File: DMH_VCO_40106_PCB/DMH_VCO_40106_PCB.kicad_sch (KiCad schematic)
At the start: 0 parts

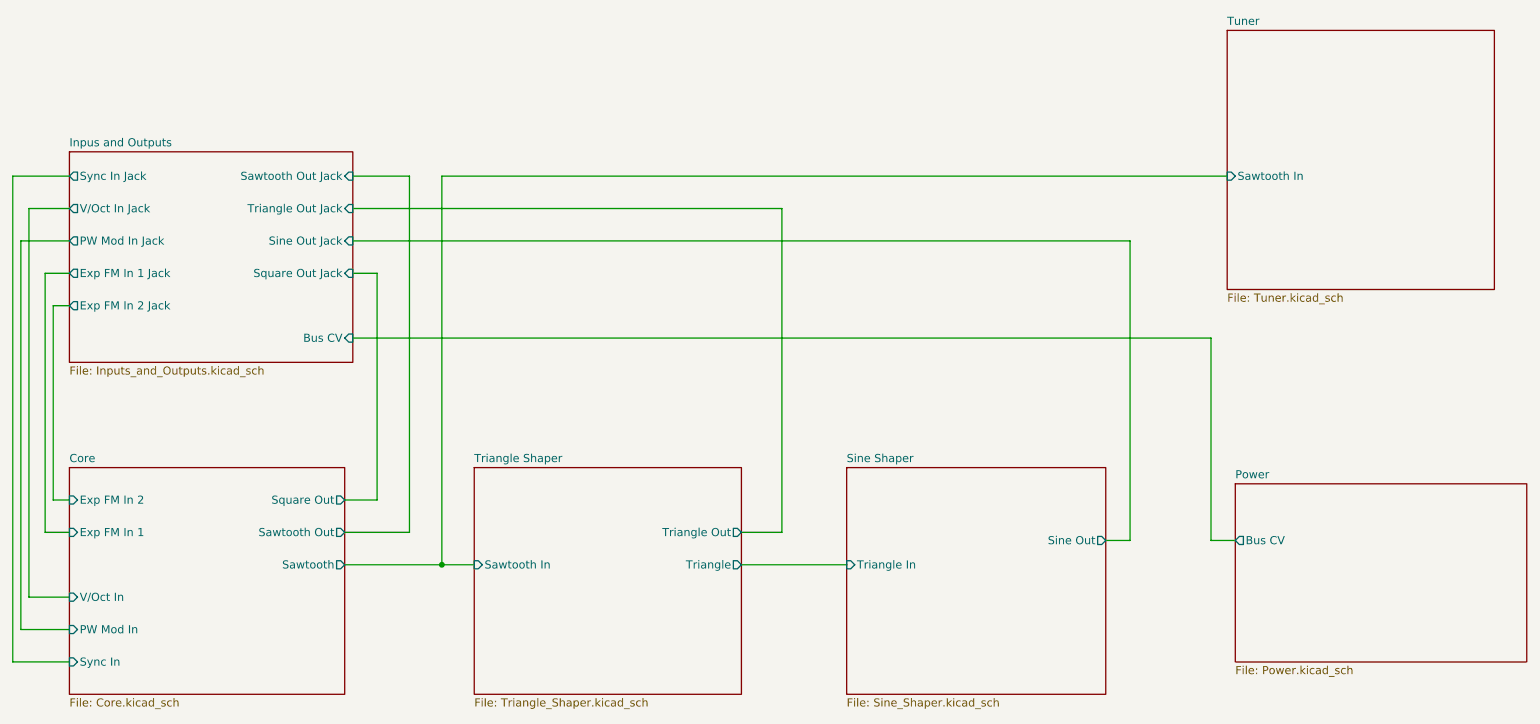
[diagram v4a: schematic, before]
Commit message: FW work in progress
Code left in state where fixed frequency point (e.g. 300Hz) is recognized, and the tuner swings from TOO LOW to TOO HIGH depending if below or above this frequency. I see a ~+10Hz offset though if checking the frequency in ableton. Also had to connect uc to square wave. Saw wave is too unstable without hysteresis.
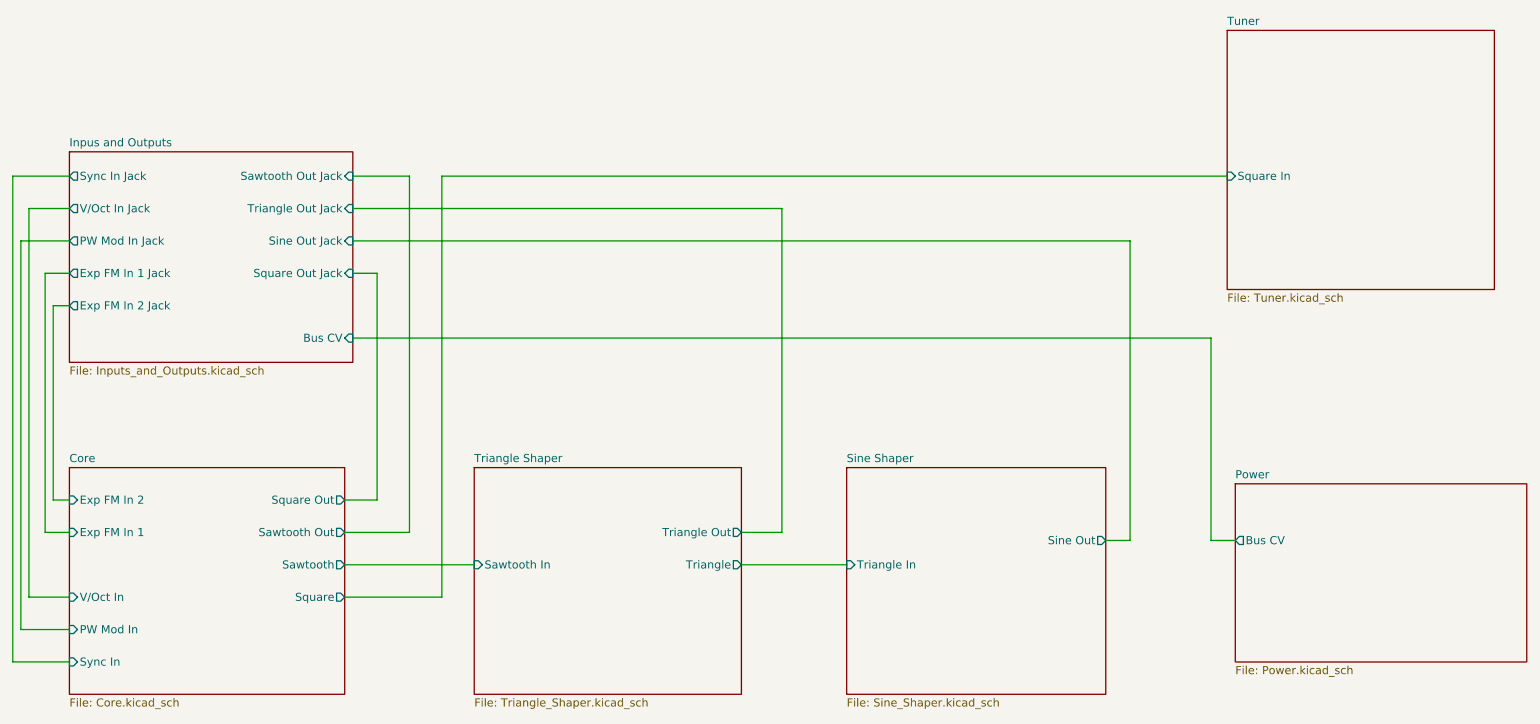
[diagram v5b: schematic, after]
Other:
- sheet Core ports: added Square; removed none
- sheet Tuner ports: added Square In; removed Sawtooth In
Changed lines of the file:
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@@
 		(company "DMH Instruments")
 	)
-	(junction
-		(at 86.36 114.3)
-		(diameter 0)
-		(color 0 0 0 0)
-	)
 	(wire
 		(pts
@@
 	(wire
 		(pts
+			(xy 86.36 119.38) (xy 86.36 53.34)
+		)
+		(stroke
+			(width 0)
+			(type default)
+		)
+	)
+	(wire
+		(pts
 			(xy 27.94 53.34) (xy 19.05 53.34)
 		)
@@
 	(wire
 		(pts
+			(xy 71.12 119.38) (xy 86.36 119.38)
+		)
+		(stroke
+			(width 0)
+			(type default)
+		)
+	)
+	(wire
+		(pts
 			(xy 25.4 104.14) (xy 27.94 104.14)
 		)
@@
 	(wire
 		(pts
-			(xy 209.55 53.34) (xy 86.36 53.34)
-		)
-		(stroke
-			(width 0)
-			(type default)
-		)
-	)
-	(wire
-		(pts
 			(xy 139.7 109.22) (xy 133.35 109.22)
 		)
@@
 	(wire
 		(pts
-			(xy 86.36 53.34) (xy 86.36 114.3)
-		)
-		(stroke
-			(width 0)
-			(type default)
-		)
-	)
-	(wire
-		(pts
 			(xy 27.94 68.58) (xy 24.13 68.58)
 		)
@@
 	(wire
 		(pts
+			(xy 86.36 53.34) (xy 209.55 53.34)
+		)
+		(stroke
+			(width 0)
+			(type default)
+		)
+	)
+	(wire
+		(pts
 			(xy 71.12 109.22) (xy 81.28 109.22)
 		)
@@
 	(wire
 		(pts
-			(xy 71.12 114.3) (xy 86.36 114.3)
+			(xy 71.12 114.3) (xy 91.44 114.3)
 		)
 		(stroke
@@
 		(pts
 			(xy 20.32 124.46) (xy 20.32 63.5)
-		)
-		(stroke
-			(width 0)
-			(type default)
-		)
-	)
-	(wire
-		(pts
-			(xy 86.36 114.3) (xy 91.44 114.3)
 		)
 		(stroke
@@
 			)
 		)
+		(pin "Square" output
+			(at 71.12 119.38 0)
+			(effects
+				(font
+					(size 1.27 1.27)
+				)
+				(justify right)
+			)
+		)
 		(instances
 			(project "DMH_VCO_40106_PCB"
@@
 			)
 		)
-		(pin "Sawtooth In" input
+		(pin "Square In" input
 			(at 209.55 53.34 180)
 			(effects
